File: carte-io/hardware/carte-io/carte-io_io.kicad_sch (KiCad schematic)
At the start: 2 parts, among them J1 USB_C_Receptacle_USB2.0_14P, U2 FT231XQ

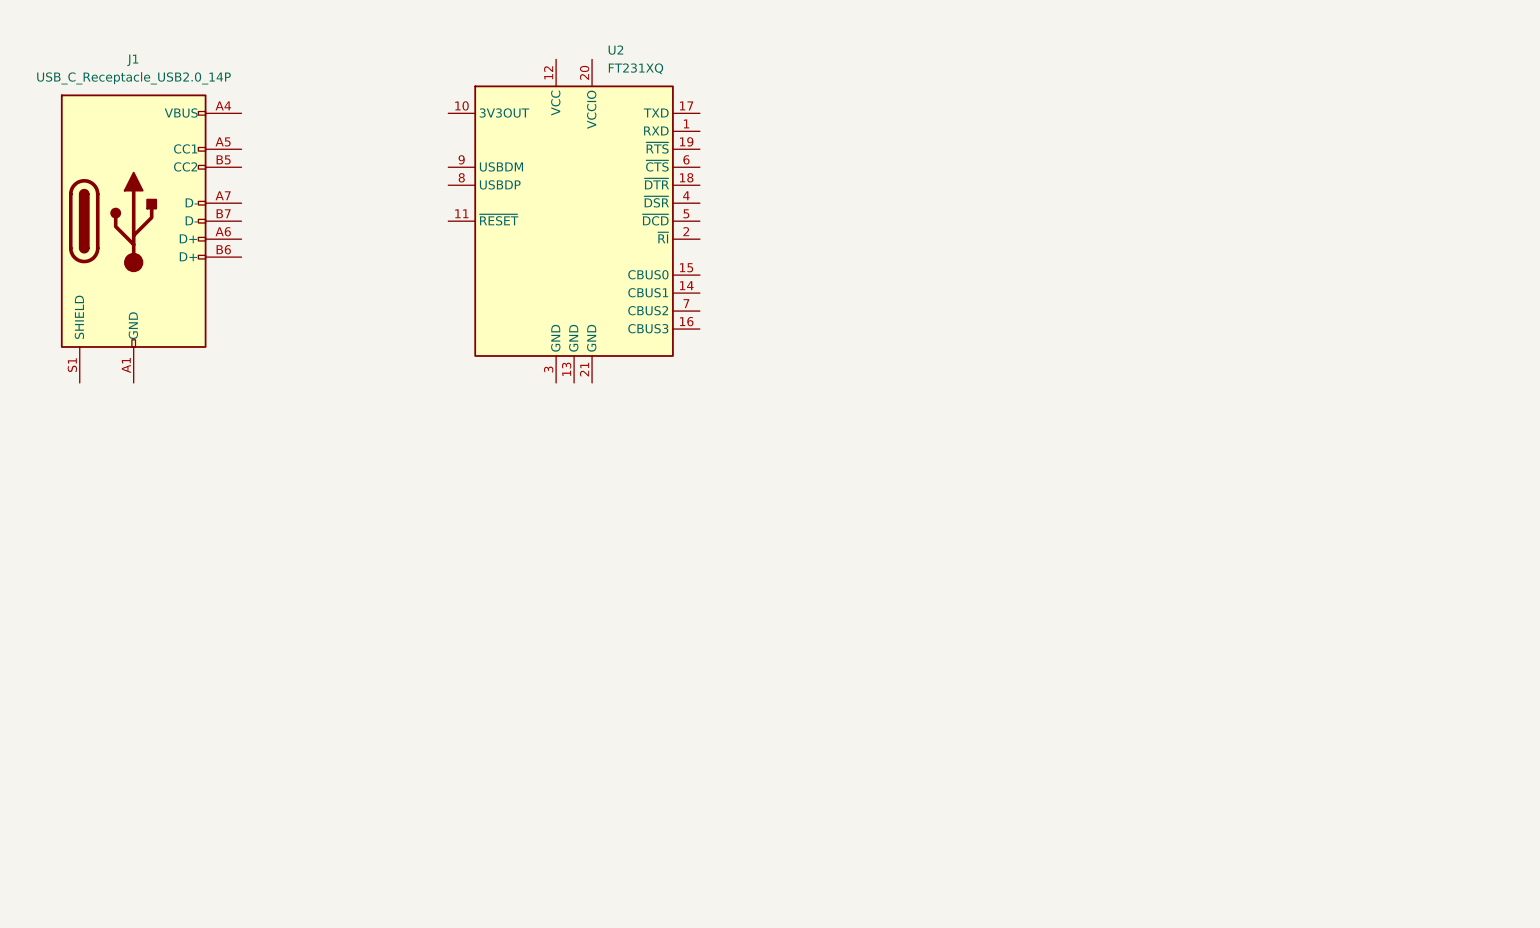
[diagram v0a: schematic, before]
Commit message: Selection de differents connecteurs
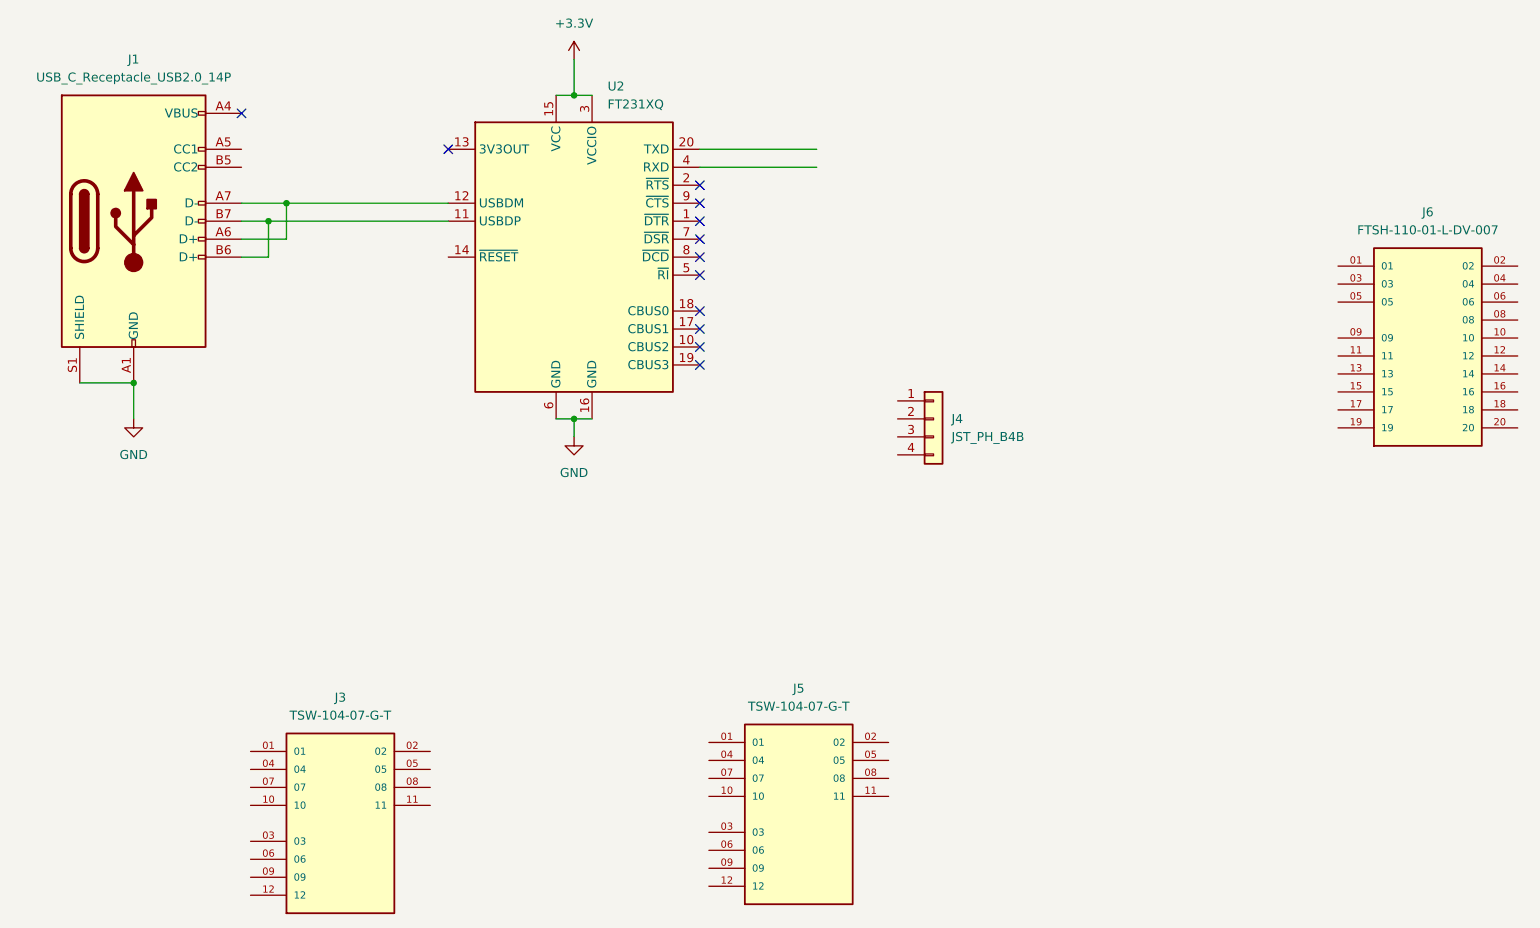
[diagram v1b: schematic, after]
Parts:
- added J3, J5: TSW-104-07-G-T, TSW-104-07-G-T:SAMTEC_TSW-104-07-G-T, symbol TSW-104-07-G-T:TSW-104-07-G-T
- added J4: JST_PH_B4B, Connector_JST:JST_PH_B4B-PH-K_1x04_P2.00mm_Vertical, symbol Connector_Generic:Conn_01x04
- added J6: FTSH-110-01-L-DV-007, FTSH-110-01-L-DV-007:SAMTEC_FTSH-110-01-L-DV-007, symbol FTSH-110-01-L-DV-007:FTSH-110-01-L-DV-007
- U2: footprint Package_DFN_QFN:QFN-20-1EP_4x4mm_P0.5mm_EP2.5x2.5mm -> Package_SO:SSOP-20_3.9x8.7mm_P0.635mm; symbol Interface_USB:FT231XQ -> Interface_USB:FT231XS
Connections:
- net GND: now reaches J1.A1 (GND), J1.A12 (GND), J1.B1 (GND), J1.B12 (GND)
- net GND: now also J1.S1 (SHIELD), U2.16 (GND), U2.6 (GND)
- net at J1.A6 (D+): now also J1.A7 (D-), U2.12 (USBDM)
- net at J1.B6 (D+): now also J1.B7 (D-), U2.11 (USBDP)
- net +3.3V: now reaches U2.15 (VCC)
- net +3.3V: now also U2.3 (VCCIO)
- no-connect marks 0 -> 12
